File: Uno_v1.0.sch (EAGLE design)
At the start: 58 parts, among them CN1 POWER_JACK, CN2 47346-0001, IC1 AMS1117-5.0, IC2 AMS1117-3.3, IC3 MCP6002T-I/SN, J1 ICSP, J2 Digital2, J3 Digital1, J4 POWER, J5 Analog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

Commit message: Add some traces
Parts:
- C10, C11, C12, C13, C14, C15, C16, C18, C19, C4, C5, C6, C7, C8, C9: device rcl:C-EUC0603 -> rcl:C-EUC0402
- R1, R10, R11, R12, R2, R3, R4, R5, R6, R7, R8, R9: device rcl:R-EU_R0603 -> rcl:R-EU_R0402
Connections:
- new net USB_SHIELD: CN2.SHIELD

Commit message: Add some wires. Add top/bottom fills. Add top/bottom silks. Add pin descriptions.
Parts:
- added LOGO1: MFDECLOGO_SQ_10MM, _my_logos:MFDECLOGO_SQ_10MM
- added LOGO2: MFDECLOGO_L_40MM, _my_logos:MFDECLOGO_L_40MM
- renumbered J1 to CN5, J2 to CN3, J3 to CN4, J4 to CN6, J5 to CN7

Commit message: Minor adjustments
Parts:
- CN3: value Digital2 -> DIGITAL10
- CN4: value Digital1 -> DIGITAL8
- CN6: value POWER -> POWER8
- CN7: value Analog -> ANALOG6
- T1: value PMOSFET -> AO3401A
- U2: value ATMEGA328P_TQFP -> ATMEGA328P-AU
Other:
- moved on the sheet: C8
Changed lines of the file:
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@@
 <part name="GND5" library="SparkFun-PowerSymbols" library_urn="urn:adsk.eagle:library:530" deviceset="GND" device=""/>
 <part name="IC3" library="linear" library_urn="urn:adsk.eagle:library:262" deviceset="LMV358?*" device="M" package3d_urn="urn:adsk.eagle:package:16404/2" technology="X" value="MCP6002T-I/SN"/>
-<part name="T1" library="Transistor" library_urn="urn:adsk.eagle:library:16378713" deviceset="PMOSFET" device="SOT23" package3d_urn="urn:adsk.eagle:package:28738/2" technology="_" value="PMOSFET"/>
+<part name="T1" library="Transistor" library_urn="urn:adsk.eagle:library:16378713" deviceset="PMOSFET" device="SOT23" package3d_urn="urn:adsk.eagle:package:28738/2" technology="_" value="AO3401A"/>
 <part name="R4" library="rcl" library_urn="urn:adsk.eagle:library:334" deviceset="R-EU_" device="R0402" package3d_urn="urn:adsk.eagle:package:23547/3" value="100K"/>
 <part name="R5" library="rcl" library_urn="urn:adsk.eagle:library:334" deviceset="R-EU_" device="R0402" package3d_urn="urn:adsk.eagle:package:23547/3" value="100K"/>
@@
 <part name="GND9" library="SparkFun-PowerSymbols" library_urn="urn:adsk.eagle:library:530" deviceset="GND" device=""/>
 <part name="FRAME2" library="frames" library_urn="urn:adsk.eagle:library:229" deviceset="DINA4_L" device=""/>
-<part name="U2" library="SparkFun-IC-Microcontroller" library_urn="urn:adsk.eagle:library:525" deviceset="ATMEGA328P_TQFP" device="" package3d_urn="urn:adsk.eagle:package:38945/1" value="ATMEGA328P_TQFP"/>
+<part name="U2" library="SparkFun-IC-Microcontroller" library_urn="urn:adsk.eagle:library:525" deviceset="ATMEGA328P_TQFP" device="" package3d_urn="urn:adsk.eagle:package:38945/1" value="ATMEGA328P-AU"/>
 <part name="Q2" library="crystal-geyer_V1_0" library_urn="urn:adsk.eagle:library:203" deviceset="KX" device="-7" package3d_urn="urn:adsk.eagle:package:11924/1" value="16MHz"/>
 <part name="R6" library="rcl" library_urn="urn:adsk.eagle:library:334" deviceset="R-EU_" device="R0402" package3d_urn="urn:adsk.eagle:package:23547/3" value="1M"/>
@@
 <part name="SUPPLY13" library="SparkFun-PowerSymbols" library_urn="urn:adsk.eagle:library:530" deviceset="5V" device=""/>
 <part name="CN5" library="SparkFun-Connectors" deviceset="CONN_03X2" device="NO_SILK" value="ICSP"/>
-<part name="CN3" library="SparkFun-Connectors" deviceset="CONN_10" device="NO_SILK_PTH_FEMALE" value="Digital2"/>
-<part name="CN4" library="SparkFun-Connectors" deviceset="CONN_08" device="NO_SILK_FEMALE_PTH" value="Digital1"/>
-<part name="CN6" library="SparkFun-Connectors" deviceset="CONN_08" device="NO_SILK_FEMALE_PTH" value="POWER"/>
-<part name="CN7" library="SparkFun-Connectors" deviceset="CONN_06" device="NO_SILK_FEMALE_PTH" value="Analog"/>
+<part name="CN3" library="SparkFun-Connectors" deviceset="CONN_10" device="NO_SILK_PTH_FEMALE" value="DIGITAL10"/>
+<part name="CN4" library="SparkFun-Connectors" deviceset="CONN_08" device="NO_SILK_FEMALE_PTH" value="DIGITAL8"/>
+<part name="CN6" library="SparkFun-Connectors" deviceset="CONN_08" device="NO_SILK_FEMALE_PTH" value="POWER8"/>
+<part name="CN7" library="SparkFun-Connectors" deviceset="CONN_06" device="NO_SILK_FEMALE_PTH" value="ANALOG6"/>
 <part name="GND12" library="SparkFun-PowerSymbols" library_urn="urn:adsk.eagle:library:530" deviceset="GND" device=""/>
 <part name="SUPPLY14" library="SparkFun-PowerSymbols" library_urn="urn:adsk.eagle:library:530" deviceset="5V" device=""/>
@@
 <attribute name="VALUE" x="175.26" y="84.074" size="1.778" layer="96"/>
 </instance>
-<instance part="C8" gate="G$1" x="231.14" y="71.12" smashed="yes">
-<attribute name="NAME" x="232.664" y="71.501" size="1.778" layer="95"/>
-<attribute name="VALUE" x="232.664" y="66.421" size="1.778" layer="96"/>
-</instance>
-<instance part="SUPPLY6" gate="G$1" x="231.14" y="76.2" smashed="yes">
-<attribute name="VALUE" x="231.14" y="78.994" size="1.778" layer="96"/>
-</instance>
-<instance part="GND4" gate="1" x="231.14" y="60.96" smashed="yes">
-<attribute name="VALUE" x="228.6" y="58.166" size="1.778" layer="96"/>
+<instance part="C8" gate="G$1" x="226.06" y="71.12" smashed="yes">
+<attribute name="NAME" x="227.584" y="71.501" size="1.778" layer="95"/>
+<attribute name="VALUE" x="227.584" y="66.421" size="1.778" layer="96"/>
+</instance>
+<instance part="SUPPLY6" gate="G$1" x="226.06" y="76.2" smashed="yes">
+<attribute name="VALUE" x="226.06" y="78.994" size="1.778" layer="96"/>
+</instance>
+<instance part="GND4" gate="1" x="226.06" y="60.96" smashed="yes">
+<attribute name="VALUE" x="223.52" y="58.166" size="1.778" layer="96"/>
 </instance>
 <instance part="Q1" gate="G$1" x="127" y="71.12" smashed="yes" rot="R90">
@@
 <pinref part="C8" gate="G$1" pin="2"/>
 <pinref part="GND4" gate="1" pin="GND"/>
-<wire x1="231.14" y1="63.5" x2="231.14" y2="66.04" width="0.1524" layer="91"/>
+<wire x1="226.06" y1="63.5" x2="226.06" y2="66.04" width="0.1524" layer="91"/>
 </segment>
 <segment>
@@
 <pinref part="C8" gate="G$1" pin="1"/>
 <pinref part="SUPPLY6" gate="G$1" pin="5V"/>
-<wire x1="231.14" y1="76.2" x2="231.14" y2="73.66" width="0.1524" layer="91"/>
-</segment>
-<segment>
+<wire x1="226.06" y1="76.2" x2="226.06" y2="73.66" width="0.1524" layer="91"/>
+</segment>
+<segment>

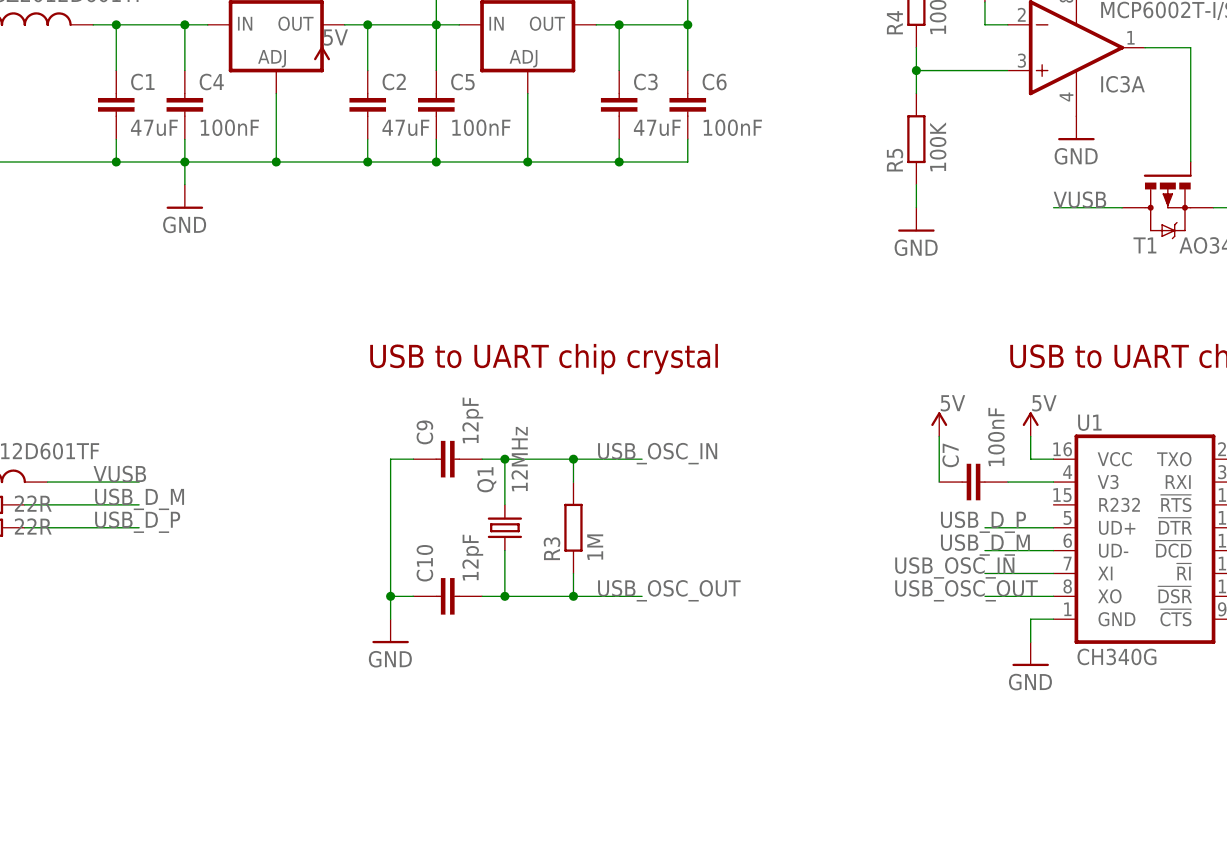
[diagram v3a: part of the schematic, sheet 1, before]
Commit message: Fix connection of V3 pin of CH340G
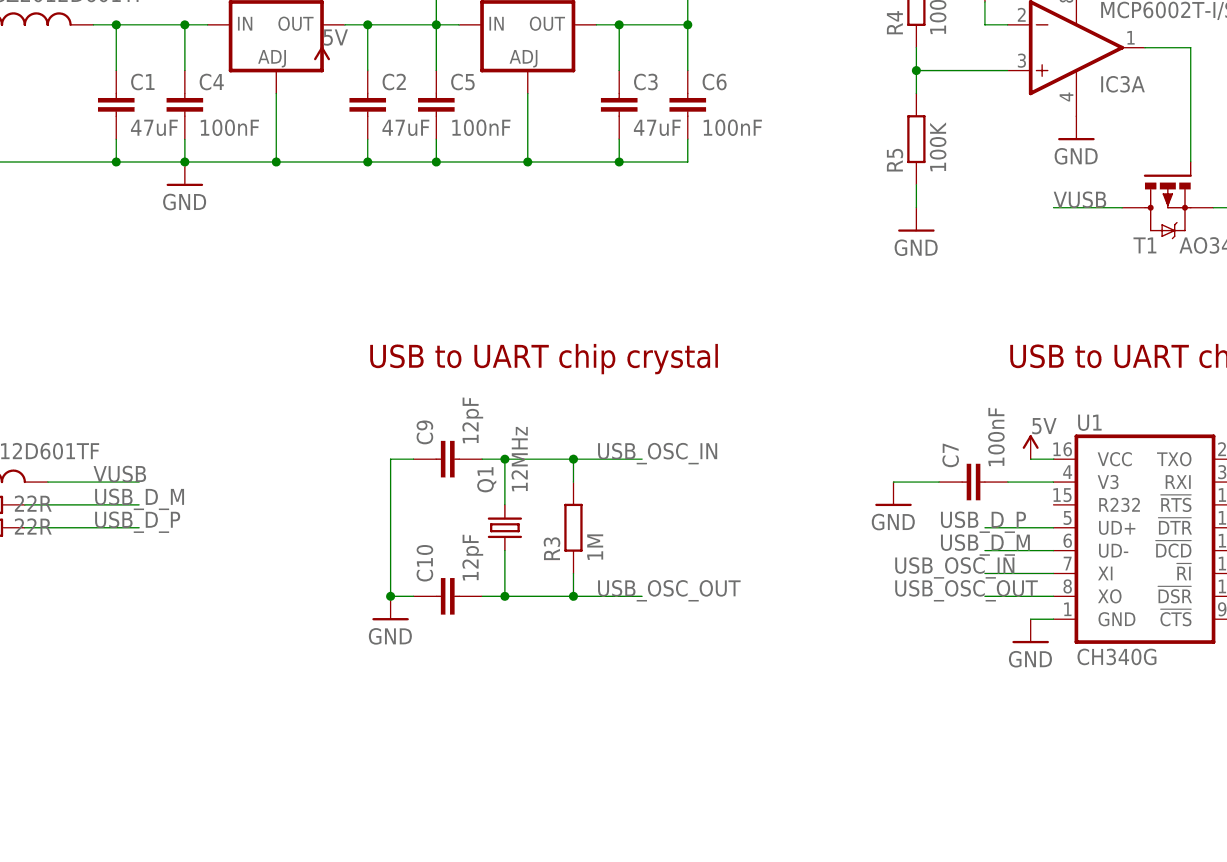
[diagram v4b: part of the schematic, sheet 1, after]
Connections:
- net 5V: no longer C7.1
- net GND: now also C7.1
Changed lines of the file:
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@@
 <part name="SUPPLY4" library="SparkFun-PowerSymbols" library_urn="urn:adsk.eagle:library:530" deviceset="5V" device=""/>
 <part name="C7" library="rcl" library_urn="urn:adsk.eagle:library:334" deviceset="C-EU" device="C0402" package3d_urn="urn:adsk.eagle:package:23626/2" value="100nF"/>
-<part name="SUPPLY5" library="SparkFun-PowerSymbols" library_urn="urn:adsk.eagle:library:530" deviceset="5V" device=""/>
 <part name="C8" library="rcl" library_urn="urn:adsk.eagle:library:334" deviceset="C-EU" device="C0402" package3d_urn="urn:adsk.eagle:package:23626/2" value="100nF"/>
 <part name="SUPPLY6" library="SparkFun-PowerSymbols" library_urn="urn:adsk.eagle:library:530" deviceset="5V" device=""/>
@@
 <part name="LOGO1" library="_my_logos" deviceset="MFDECLOGO" device="_SQ_10MM" value="MFDECLOGO_SQ_10MM"/>
 <part name="LOGO2" library="_my_logos" deviceset="MFDECLOGO" device="_L_40MM"/>
+<part name="GND24" library="SparkFun-PowerSymbols" library_urn="urn:adsk.eagle:library:530" deviceset="GND" device=""/>
 </parts>
 <sheets>
@@
 <attribute name="VALUE" x="144.78" y="134.874" size="1.778" layer="96"/>
 </instance>
-<instance part="GND1" gate="1" x="91.44" y="106.68" smashed="yes">
-<attribute name="VALUE" x="88.9" y="103.886" size="1.778" layer="96"/>
+<instance part="GND1" gate="1" x="91.44" y="109.22" smashed="yes">
+<attribute name="VALUE" x="88.9" y="106.426" size="1.778" layer="96"/>
 </instance>
 <instance part="SUPPLY1" gate="G$1" x="35.56" y="132.08" smashed="yes">
@@
 <attribute name="VALUE" x="190.5" y="55.88" size="1.778" layer="96"/>
 </instance>
-<instance part="GND3" gate="1" x="185.42" y="55.88" smashed="yes">
-<attribute name="VALUE" x="182.88" y="53.086" size="1.778" layer="96"/>
-</instance>
-<instance part="SUPPLY4" gate="G$1" x="185.42" y="81.28" smashed="yes">
-<attribute name="VALUE" x="185.42" y="84.074" size="1.778" layer="96"/>
+<instance part="GND3" gate="1" x="185.42" y="58.42" smashed="yes">
+<attribute name="VALUE" x="182.88" y="55.626" size="1.778" layer="96"/>
+</instance>
+<instance part="SUPPLY4" gate="G$1" x="185.42" y="78.74" smashed="yes">
+<attribute name="VALUE" x="185.42" y="81.534" size="1.778" layer="96"/>
 </instance>
 <instance part="C7" gate="G$1" x="177.8" y="76.2" smashed="yes" rot="R90">
@@
 <attribute name="VALUE" x="182.499" y="77.724" size="1.778" layer="96" rot="R90"/>
 </instance>
-<instance part="SUPPLY5" gate="G$1" x="175.26" y="81.28" smashed="yes">
-<attribute name="VALUE" x="175.26" y="84.074" size="1.778" layer="96"/>
-</instance>
 <instance part="C8" gate="G$1" x="226.06" y="71.12" smashed="yes">
 <attribute name="NAME" x="227.584" y="71.501" size="1.778" layer="95"/>
@@
 <attribute name="VALUE" x="124.079" y="65.024" size="1.778" layer="96" rot="R90"/>
 </instance>
-<instance part="GND5" gate="1" x="114.3" y="58.42" smashed="yes">
-<attribute name="VALUE" x="111.76" y="55.626" size="1.778" layer="96"/>
+<instance part="GND5" gate="1" x="114.3" y="60.96" smashed="yes">
+<attribute name="VALUE" x="111.76" y="58.166" size="1.778" layer="96"/>
 </instance>
 <instance part="IC3" gate="A" x="190.5" y="124.46" smashed="yes" rot="MR180">
@@
 <instance part="LOGO1" gate="G$1" x="236.22" y="25.4" smashed="yes"/>
 <instance part="LOGO2" gate="G$1" x="208.28" y="25.4" smashed="yes"/>
+<instance part="GND24" gate="1" x="170.18" y="73.66" smashed="yes">
+<attribute name="VALUE" x="167.64" y="70.866" size="1.778" layer="96"/>
+</instance>
 </instances>
 <busses>
@@
 <pinref part="C4" gate="G$1" pin="2"/>
 <wire x1="91.44" y1="114.3" x2="91.44" y2="111.76" width="0.1524" layer="91"/>
-<wire x1="91.44" y1="111.76" x2="91.44" y2="109.22" width="0.1524" layer="91"/>
 <wire x1="91.44" y1="111.76" x2="101.6" y2="111.76" width="0.1524" layer="91"/>
 <junction x="91.44" y="111.76"/>
@@
 <pinref part="U1" gate="U1" pin="GND"/>
 <wire x1="187.96" y1="60.96" x2="185.42" y2="60.96" width="0.1524" layer="91"/>
-<wire x1="185.42" y1="60.96" x2="185.42" y2="58.42" width="0.1524" layer="91"/>
 <pinref part="GND3" gate="1" pin="GND"/>
 </segment>
@@
 <pinref part="C10" gate="G$1" pin="1"/>
 <wire x1="114.3" y1="63.5" x2="116.84" y2="63.5" width="0.1524" layer="91"/>
-<wire x1="114.3" y1="63.5" x2="114.3" y2="60.96" width="0.1524" layer="91"/>
 <junction x="114.3" y="63.5"/>
 <pinref part="GND5" gate="1" pin="GND"/>
@@
 <pinref part="GND9" gate="1" pin="GND"/>
 <wire x1="210.82" y1="119.38" x2="210.82" y2="121.92" width="0.1524" layer="91"/>
+</segment>
+<segment>
+<pinref part="C7" gate="G$1" pin="1"/>
+<wire x1="175.26" y1="76.2" x2="170.18" y2="76.2" width="0.1524" layer="91"/>
+<pinref part="GND24" gate="1" pin="GND"/>
 </segment>
 </net>
@@
 <pinref part="U1" gate="U1" pin="VCC"/>
 <wire x1="187.96" y1="78.74" x2="185.42" y2="78.74" width="0.1524" layer="91"/>
-<wire x1="185.42" y1="78.74" x2="185.42" y2="81.28" width="0.1524" layer="91"/>
 <pinref part="SUPPLY4" gate="G$1" pin="5V"/>
 </segment>
 <segment>
-<pinref part="C7" gate="G$1" pin="1"/>
-<wire x1="175.26" y1="76.2" x2="175.26" y2="81.28" width="0.1524" layer="91"/>
-<pinref part="SUPPLY5" gate="G$1" pin="5V"/>
-</segment>
-<segment>

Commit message: Change capacitor sizes. Move stuff around.
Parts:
- C1, C2, C3: device rcl:C-EUC0805 -> rcl:C-EUC1206
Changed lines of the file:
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@@
 <part name="L1" library="Wurth_Automotive_WE-CBA" library_urn="urn:adsk.eagle:library:14076691" deviceset="WE-CBA_0805" device="_HC" package3d_urn="urn:adsk.eagle:package:13132996/2" technology="_782853102" value="GZ2012D601TF"/>
 <part name="F1" library="fuse" library_urn="urn:adsk.eagle:library:233" deviceset="MF-SMDF" device="" package3d_urn="urn:adsk.eagle:package:14081/1" technology="050" value="1812L050/30PR"/>
-<part name="C1" library="rcl" library_urn="urn:adsk.eagle:library:334" deviceset="C-EU" device="C0805" package3d_urn="urn:adsk.eagle:package:23617/2" value="47uF"/>
-<part name="C2" library="rcl" library_urn="urn:adsk.eagle:library:334" deviceset="C-EU" device="C0805" package3d_urn="urn:adsk.eagle:package:23617/2" value="47uF"/>
-<part name="C3" library="rcl" library_urn="urn:adsk.eagle:library:334" deviceset="C-EU" device="C0805" package3d_urn="urn:adsk.eagle:package:23617/2" value="47uF"/>
+<part name="C1" library="rcl" library_urn="urn:adsk.eagle:library:334" deviceset="C-EU" device="C1206" package3d_urn="urn:adsk.eagle:package:23618/2" value="47uF"/>
+<part name="C2" library="rcl" library_urn="urn:adsk.eagle:library:334" deviceset="C-EU" device="C1206" package3d_urn="urn:adsk.eagle:package:23618/2" value="47uF"/>
+<part name="C3" library="rcl" library_urn="urn:adsk.eagle:library:334" deviceset="C-EU" device="C1206" package3d_urn="urn:adsk.eagle:package:23618/2" value="47uF"/>
 <part name="C4" library="rcl" library_urn="urn:adsk.eagle:library:334" deviceset="C-EU" device="C0402" package3d_urn="urn:adsk.eagle:package:23626/2" value="100nF"/>
 <part name="C5" library="rcl" library_urn="urn:adsk.eagle:library:334" deviceset="C-EU" device="C0402" package3d_urn="urn:adsk.eagle:package:23626/2" value="100nF"/>

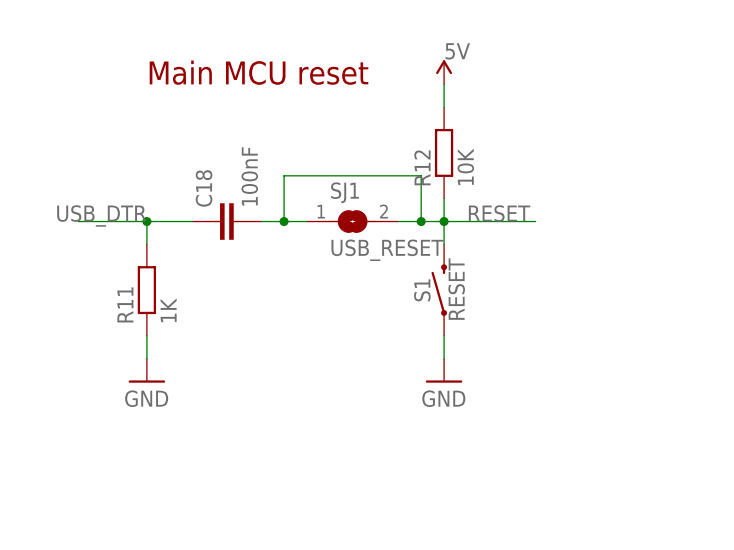
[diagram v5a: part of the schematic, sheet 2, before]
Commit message: Move stuff around. Change how SJ1 is closed by default. Add ground connections to Q2 and reset button.
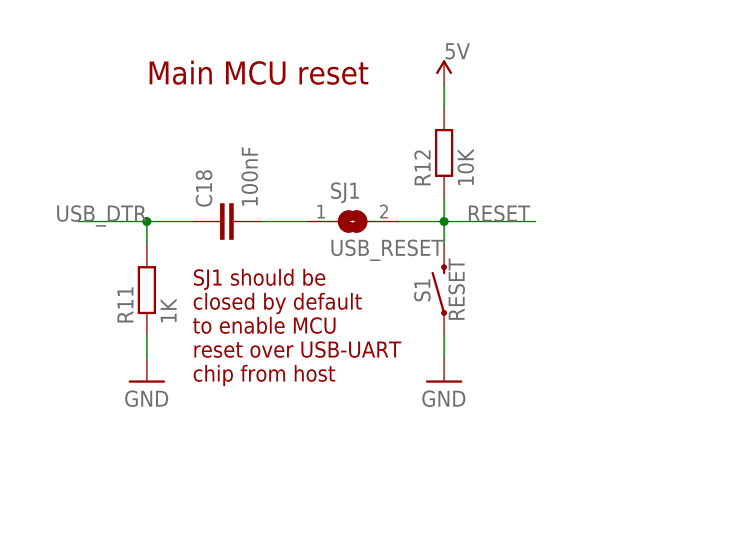
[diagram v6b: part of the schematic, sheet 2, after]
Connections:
- new net N$5: C18.2, SJ1.1
- net RESET: no longer C18.2, SJ1.1
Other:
- note added: "SJ1 should be closed by default to enable MCU reset over USB-UART chip from host"
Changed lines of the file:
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@@
 <text x="195.58" y="149.86" size="2.54" layer="94">Arduino connectors</text>
 <text x="33.02" y="101.6" size="2.54" layer="94">Main MCU crystal</text>
+<text x="35.56" y="22.86" size="1.778" layer="94">SJ1 should be
+closed by default
+to enable MCU
+reset over USB-UART
+chip from host</text>
 </plain>
 <instances>
@@
 <label x="66.04" y="40.64" size="1.778" layer="95"/>
 <pinref part="SJ1" gate="1" pin="2"/>
-<wire x1="58.42" y1="40.64" x2="60.96" y2="40.64" width="0.1524" layer="91"/>
-<wire x1="60.96" y1="40.64" x2="63.5" y2="40.64" width="0.1524" layer="91"/>
-<wire x1="60.96" y1="40.64" x2="60.96" y2="45.72" width="0.1524" layer="91"/>
-<wire x1="60.96" y1="45.72" x2="45.72" y2="45.72" width="0.1524" layer="91"/>
-<junction x="60.96" y="40.64"/>
-<pinref part="C18" gate="G$1" pin="2"/>
-<pinref part="SJ1" gate="1" pin="1"/>
-<wire x1="43.18" y1="40.64" x2="45.72" y2="40.64" width="0.1524" layer="91"/>
-<wire x1="45.72" y1="40.64" x2="48.26" y2="40.64" width="0.1524" layer="91"/>
-<wire x1="45.72" y1="45.72" x2="45.72" y2="40.64" width="0.1524" layer="91"/>
-<junction x="45.72" y="40.64"/>
+<wire x1="58.42" y1="40.64" x2="63.5" y2="40.64" width="0.1524" layer="91"/>
 </segment>
 <segment>
@@
 <junction x="30.48" y="40.64"/>
 <label x="20.32" y="40.64" size="1.778" layer="95"/>
+</segment>
+</net>
+<net name="N$5" class="0">
+<segment>
+<pinref part="SJ1" gate="1" pin="1"/>
+<pinref part="C18" gate="G$1" pin="2"/>
+<wire x1="43.18" y1="40.64" x2="48.26" y2="40.64" width="0.1524" layer="91"/>
 </segment>
 </net>
@@
 </drawing>
 <compatibility>
+<note version="6.3" minversion="6.2.2" severity="warning">
+Since Version 6.2.2 text objects can contain more than one line,
+which will not be processed correctly with this version.
+</note>
 <note version="8.2" severity="warning">
 Since Version 8.2, EAGLE supports online libraries. The ids
